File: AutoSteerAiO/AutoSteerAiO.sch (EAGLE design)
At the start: 81 parts, among them J4 CONNECTOR 1x5 PINS, K4 CB1A-P-12V, T1 BC547, U1 VX7805-1000

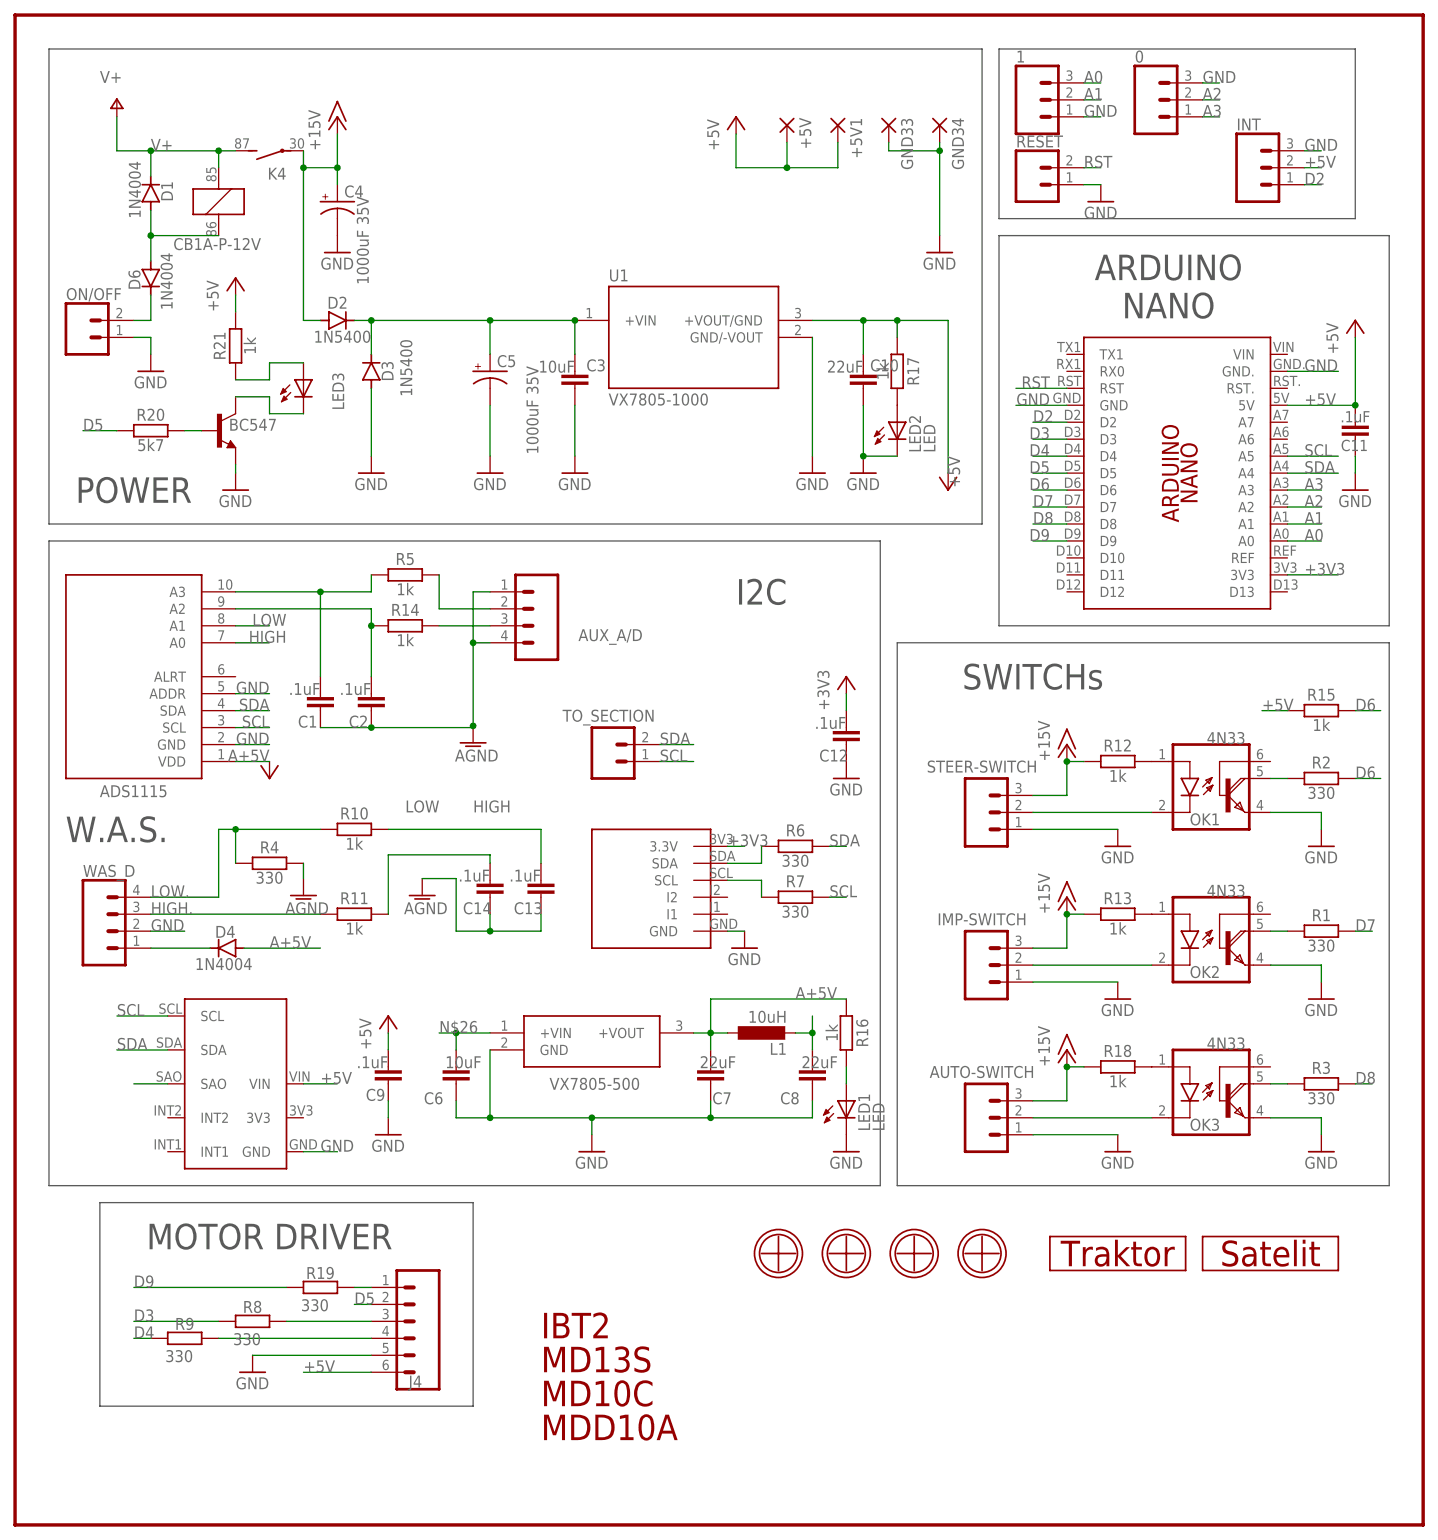
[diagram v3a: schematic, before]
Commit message: Add files via upload
Added Connector for Encoder, 8 pins connector for IBT2 to be able to connect with Flat ribbon cable...
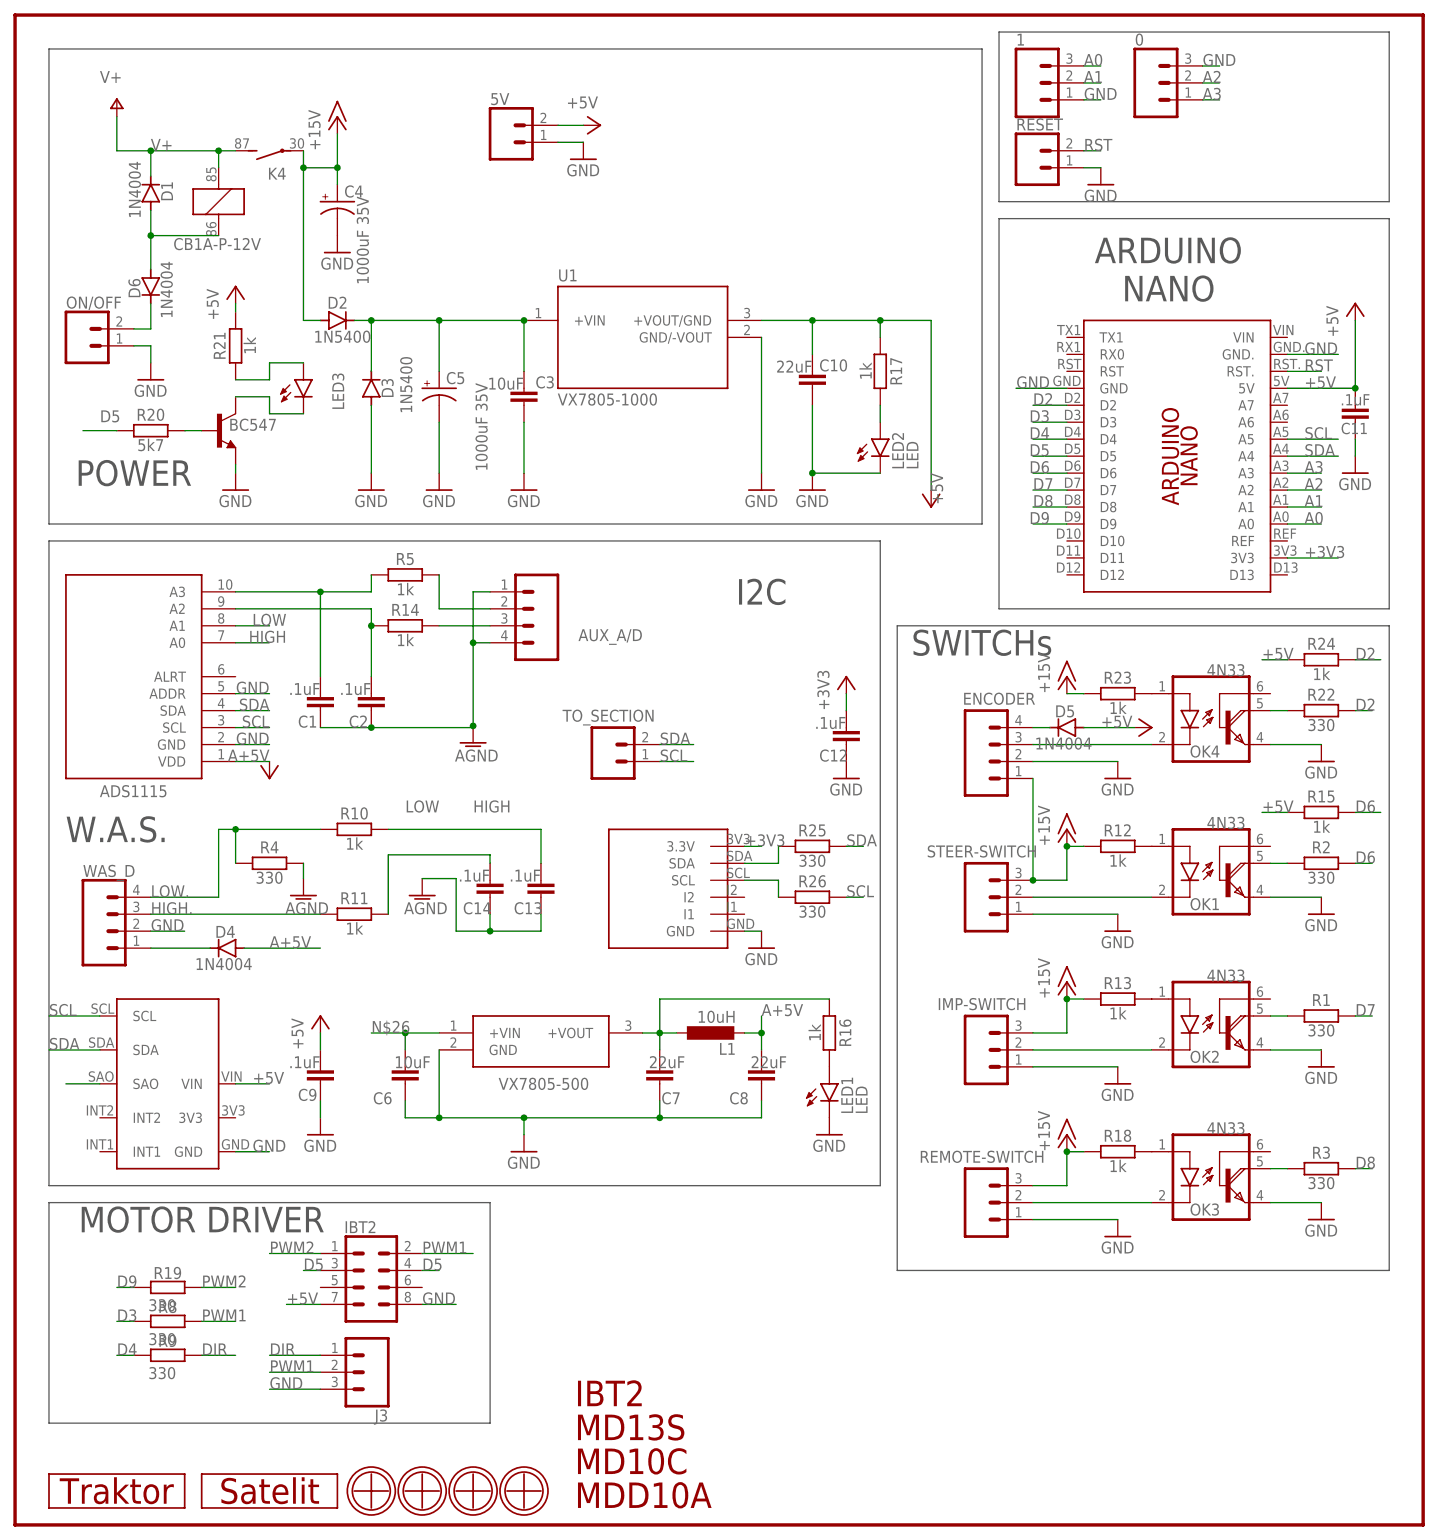
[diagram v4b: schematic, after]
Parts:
- removed +5V, +5V1, GND33, GND34: (no value), wirepad:2,15/1,0
- removed AUTO-SWITCH: CONNECTOR 1x3 PINS, SparkFun-Connectors:CONN_03
- removed INT: (no value), SparkFun-Connectors:CONN_03
- removed J4: CONNECTOR 1x5 PINS, SparkFun-Connectors:CONN_06SILK_FEMALE_PTH
- removed R6, R7: 330, resistor:R-EU_0207/7
- added 5V: CONNECTOR 1x2 PINS, SparkFun-Connectors:CONN_02
- added D5: 1N4004, diode:1N4004
- added ENCODER: CONNECTOR 1x3 PINS, SparkFun-Connectors:CONN_04
- added IBT2: (no value), SparkFun-Connectors:CONN_04X2
- added J3: (no value), SparkFun-Connectors:CONN_03
- added OK4: 4N33, #optocoupler:4N33
- added R22, R25, R26: 330, resistor:R-EU_0207/7
- added R23, R24: 1k, resistor:R-EU_0207/7
- added REMOTE-SWITCH: CONNECTOR 1x3 PINS, SparkFun-Connectors:CONN_03
- LED1, LED2, LED3: device adafruit:LED5MM -> led:LED3MM
- OK1, OK2, OK3: device optocoupler:4N33 -> #optocoupler:4N33
- T1: OC_NEWARK (none) -> unknown
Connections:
- removed net N$1: R6.1, U$13.SDA
- removed net N$22: J4.1, R19.1
- removed net N$9: R7.1, U$13.SCL
- new net DIR: J3.1, R9.1
- new net N$29: OK4.COL, R22.1
- new net N$30: OK4.A, R23.2
- new net N$31: ENCODER.3, OK4.C
- new net N$32: D5.C, ENCODER.4
- new net PWM1: IBT2.2, J3.2, R8.1
- new net PWM2: IBT2.1, R19.1
- net +15V: now also ENCODER.1, R23.1, REMOTE-SWITCH.3; no longer AUTO-SWITCH.3
- net +5V: now also 5V.2, D5.A, IBT2.7, R24.1; no longer +5V.P, +5V1.P, INT.2, J4.6
- net D2: now also R22.2, R24.2; no longer INT.1
- net D5: now also IBT2.3, IBT2.4; no longer J4.2
- net GND: now also 5V.1, ENCODER.2, IBT2.8, J3.3, OK4.E, REMOTE-SWITCH.1; no longer AUTO-SWITCH.1, GND33.P, GND34.P, INT.3, J4.5
- net N$12: now also REMOTE-SWITCH.2; no longer AUTO-SWITCH.2
- net N$19: now also R25.1, U$13.SDA; no longer J4.4, R9.1
- net N$20: now also R26.1, U$13.SCL; no longer J4.3, R8.1
- net RST: now also PCB1.RST.; no longer PCB1.RST
- net SCL: now also R26.2; no longer R7.2
- net SDA: now also R25.2; no longer R6.2
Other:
- moved on the sheet: 0, 1, C10, C11, C3, C5, C6, C7, C8, C9, D3, D6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

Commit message: Add files via upload
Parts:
- ENCODER: device SparkFun-Connectors:CONN_04 -> SparkFun-Connectors:CONN_03
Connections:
- removed net N$31: ENCODER.3, OK4.C
- removed net N$32: D5.C, ENCODER.4
- new net N$1: D5.C, ENCODER.3
- new net N$9: ENCODER.2, OK4.C
- net +15V: no longer ENCODER.1
- net GND: now also ENCODER.1; no longer ENCODER.2
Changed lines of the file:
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@@
 <attribute name="OC_NEWARK" value="unknown"/>
 </part>
-<part name="ENCODER" library="SparkFun-Connectors" library_urn="urn:adsk.eagle:library:513" deviceset="CONN_04" device="" package3d_urn="urn:adsk.eagle:package:38085/1" value="CONNECTOR 1x3 PINS">
+<part name="ENCODER" library="SparkFun-Connectors" library_urn="urn:adsk.eagle:library:513" deviceset="CONN_03" device="" package3d_urn="urn:adsk.eagle:package:38063/1" value="CONNECTOR 1x3 PINS">
 <attribute name="MF" value=""/>
 <attribute name="MPN" value=""/>
@@
 <attribute name="MPN" x="195.58" y="170.18" size="1.778" layer="96" display="off"/>
 </instance>
-<instance part="ENCODER" gate="G$1" x="147.32" y="177.8" smashed="yes">
-<attribute name="NAME" x="147.32" y="187.198" size="1.778" layer="95" font="vector" align="center"/>
-<attribute name="OC_NEWARK" x="147.32" y="177.8" size="1.778" layer="96" display="off"/>
-<attribute name="MF" x="147.32" y="177.8" size="1.778" layer="96" display="off"/>
-<attribute name="MPN" x="147.32" y="177.8" size="1.778" layer="96" display="off"/>
+<instance part="ENCODER" gate="J$1" x="144.78" y="180.34" smashed="yes">
+<attribute name="NAME" x="144.78" y="189.738" size="1.778" layer="95" font="vector" align="center"/>
+<attribute name="OC_NEWARK" x="144.78" y="180.34" size="1.778" layer="96" display="off"/>
+<attribute name="MF" x="144.78" y="180.34" size="1.778" layer="96" display="off"/>
+<attribute name="MPN" x="144.78" y="180.34" size="1.778" layer="96" display="off"/>
 </instance>
 <instance part="R22" gate="G$1" x="195.58" y="185.42" smashed="yes">
@@
 </segment>
 <segment>
-<pinref part="ENCODER" gate="G$1" pin="2"/>
-<wire x1="152.4" y1="177.8" x2="165.1" y2="177.8" width="0.1524" layer="91"/>
-<pinref part="GND22" gate="1" pin="GND"/>
-</segment>
-<segment>
 <pinref part="GND25" gate="1" pin="GND"/>
 <pinref part="5V" gate="G$1" pin="1"/>
@@
 <label x="35.56" y="119.38" size="1.778" layer="95"/>
 <pinref part="MMA8542" gate="G$1" pin="GND"/>
+</segment>
+<segment>
+<pinref part="GND22" gate="1" pin="GND"/>
+<pinref part="ENCODER" gate="J$1" pin="1"/>
+<wire x1="165.1" y1="177.8" x2="152.4" y2="177.8" width="0.1524" layer="91"/>
 </segment>
 </net>
@@
 <wire x1="157.48" y1="165.1" x2="157.48" y2="160.02" width="0.1524" layer="91"/>
 <junction x="157.48" y="165.1"/>
-<pinref part="ENCODER" gate="G$1" pin="1"/>
-<wire x1="152.4" y1="160.02" x2="152.4" y2="175.26" width="0.1524" layer="91"/>
-<junction x="152.4" y="160.02"/>
 </segment>
 <segment>
@@
 </segment>
 </net>
-<net name="N$31" class="0">
-<segment>
-<pinref part="OK4" gate="A" pin="C"/>
-<pinref part="ENCODER" gate="G$1" pin="3"/>
-<wire x1="170.18" y1="180.34" x2="152.4" y2="180.34" width="0.1524" layer="91"/>
-</segment>
-</net>
-<net name="N$32" class="0">
-<segment>
-<pinref part="ENCODER" gate="G$1" pin="4"/>
-<wire x1="154.94" y1="182.88" x2="152.4" y2="182.88" width="0.1524" layer="91"/>
-<pinref part="D5" gate="1" pin="C"/>
-</segment>
-</net>
 <net name="PWM2" class="0">
 <segment>
@@
 </segment>
 </net>
+<net name="N$1" class="0">
+<segment>
+<pinref part="D5" gate="1" pin="C"/>
+<pinref part="ENCODER" gate="J$1" pin="3"/>
+<wire x1="154.94" y1="182.88" x2="152.4" y2="182.88" width="0.1524" layer="91"/>
+</segment>
+</net>
+<net name="N$9" class="0">
+<segment>
+<pinref part="OK4" gate="A" pin="C"/>
+<pinref part="ENCODER" gate="J$1" pin="2"/>
+<wire x1="170.18" y1="180.34" x2="152.4" y2="180.34" width="0.1524" layer="91"/>
+</segment>
+</net>

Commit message: Add files via upload
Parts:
- K4: device relay:CB1A-P-12V -> #relay:CB1A-P-12V; OC_NEWARK unknown -> (none)
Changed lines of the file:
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@@
 <part name="P+11" library="supply1" library_urn="urn:adsk.eagle:library:371" deviceset="+5V" device=""/>
 <part name="OK1" library="#optocoupler" deviceset="4N33" device="" package3d_urn="urn:adsk.eagle:package:21942/1"/>
-<part name="K4" library="relay" library_urn="urn:adsk.eagle:library:339" deviceset="CB*" device="" package3d_urn="urn:adsk.eagle:package:24437/1" technology="1A-P-12V">
-<attribute name="MF" value=""/>
-<attribute name="MPN" value=""/>
-<attribute name="OC_NEWARK" value="unknown"/>
-</part>
+<part name="K4" library="#relay" deviceset="CB*" device="" technology="1A-P-12V"/>
 <part name="OK2" library="#optocoupler" deviceset="4N33" device="" package3d_urn="urn:adsk.eagle:package:21942/1"/>
 <part name="OK3" library="#optocoupler" deviceset="4N33" device="" package3d_urn="urn:adsk.eagle:package:21942/1"/>
